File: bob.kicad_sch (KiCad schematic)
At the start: 49 parts, among them J1 Mini USB Female, J2 GPIO (Optional), J3 GPIO (Optional), J4 Screw Terminal, 2.54mm, J5 Conn_01x04_Male, J6 Conn_01x03_Male, U1 W25Q64JVSS, U2 AMS1117-3.3, U3 RP2040, U4 QMI8658C, U5 HP203B, U6 QMC5883L, Y1 12MHz

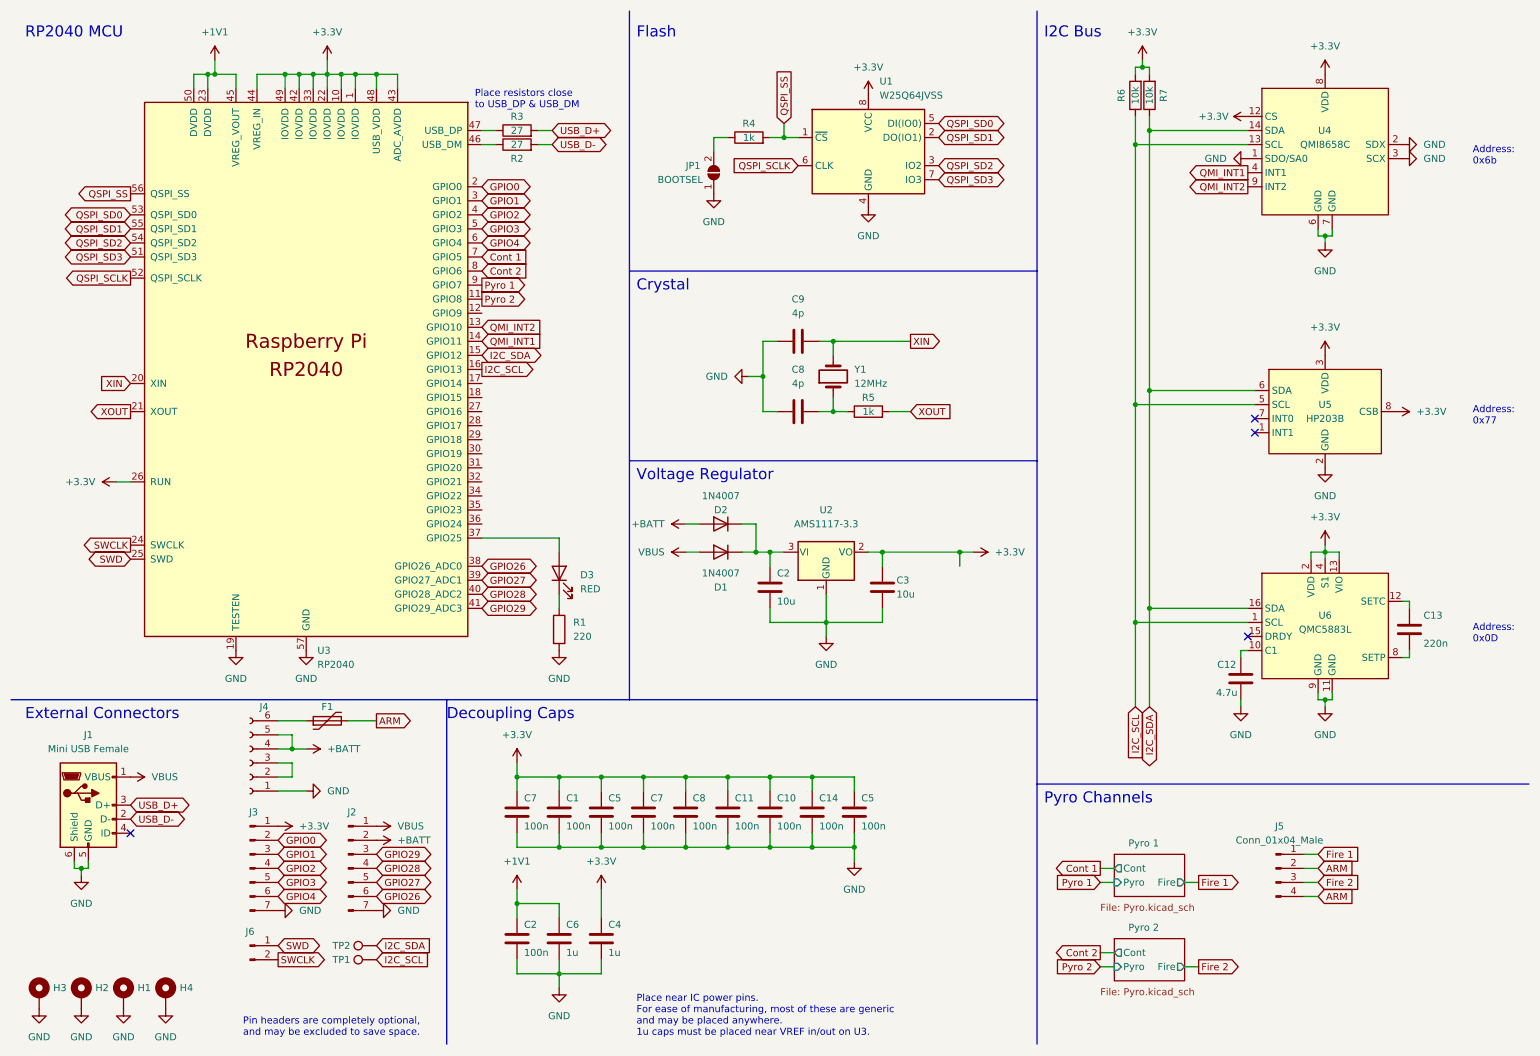
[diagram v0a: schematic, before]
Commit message: Swap out components to match LCSC stock
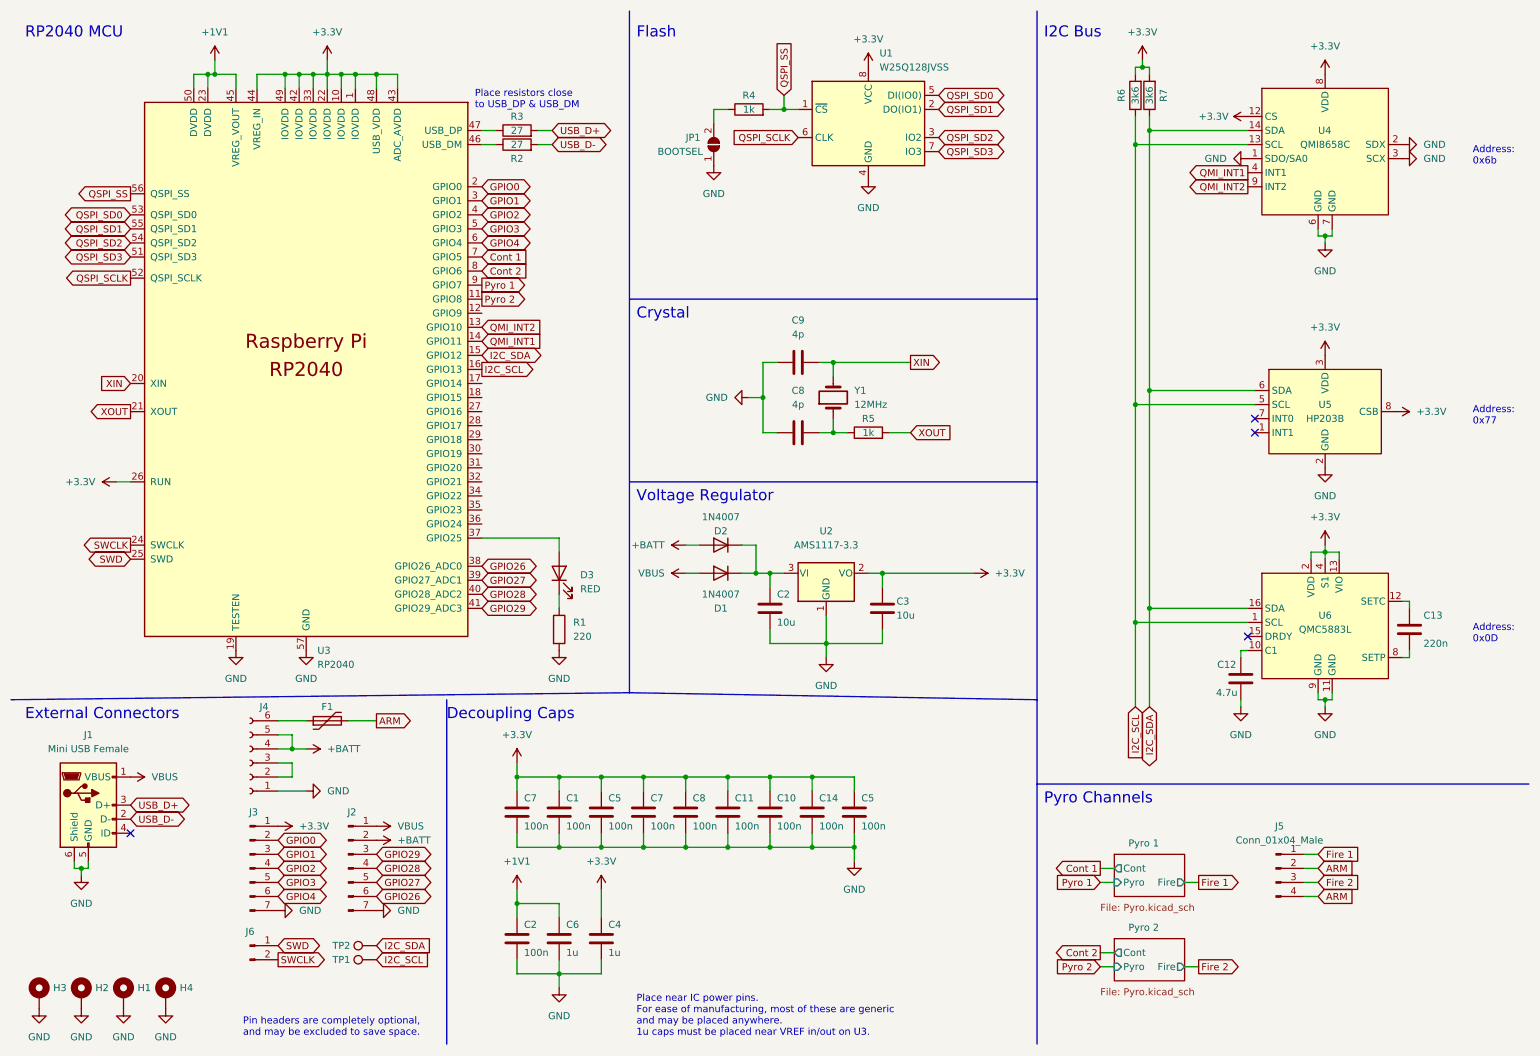
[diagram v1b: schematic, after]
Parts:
- R6, R7: value 10k -> 3k6; LCSC C25804 -> C22980
- U1: value W25Q64JVSS -> W25Q128JVSS; LCSC C83140 -> C97521
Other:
- moved on the sheet: C2, C3, C8, C9, D1, D2, JP1, R4, R5, U1, U2, Y1

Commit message: Add dedicated flash for data
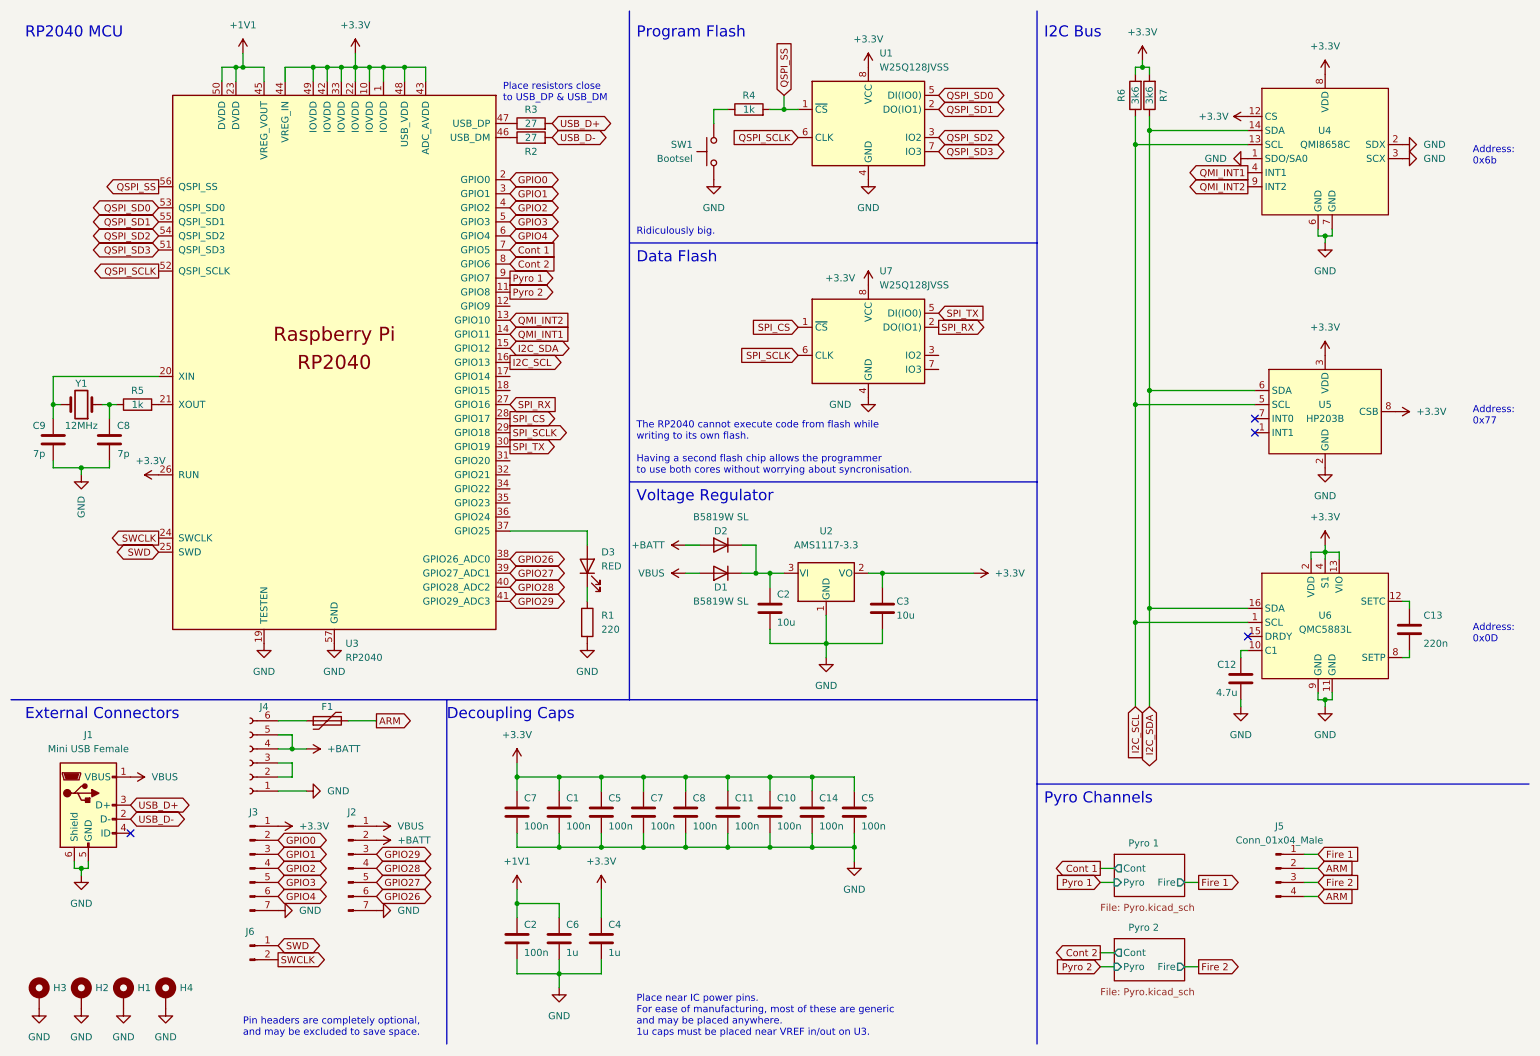
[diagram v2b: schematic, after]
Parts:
- removed JP1: BOOTSEL, Button_Switch_SMD:SW_SPST_B3U-1000P, symbol Jumper:SolderJumper_2_Open
- removed TP1, TP2: TestPoint, TestPoint:TestPoint_Pad_D1.0mm, symbol Connector:TestPoint
- added SW1: Bootsel, Button_Switch_SMD:SW_SPST_TL3342, symbol Switch:SW_Push
- added U7: W25Q128JVSS, Package_SO:SOIC-8_5.23x5.23mm_P1.27mm, symbol Memory_Flash:W25Q32JVSS
- C8, C9: value 4p -> 7p; footprint Capacitor_SMD:C_0603_1608Metric -> Capacitor_SMD:C_0402_1005Metric; JLC 0603 -> 0402; LCSC C2312234 -> C2918529
- D1, D2: value 1N4007 -> B5819W SL; LCSC C727081 -> C8598
- Y1: footprint Crystal:Crystal_SMD_5032-2Pin_5.0x3.2mm -> Crystal:Crystal_SMD_3225-4Pin_3.2x2.5mm; JLC 5032 -> SMD3225-4P
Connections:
- net +3V3: now also U7.8 (VCC)
- net GND: now also SW1.1, U7.4 (GND)
- net at R4.1: now also SW1.2
- net SPI_RX: now reaches U3.27 (GPIO16)
- net SPI_RX: now also U7.2 (DO(IO1))
- net SPI_CS: now reaches U3.28 (GPIO17)
- net SPI_CS: now also U7.1 (~{CS})
- net SPI_SCLK: now reaches U3.29 (GPIO18)
- net SPI_SCLK: now also U7.6 (CLK)
- net SPI_TX: now reaches U3.30 (GPIO19)
- net SPI_TX: now also U7.5 (DI(IO0))
- net XIN: no longer names the net of C9.2, U3.20 (XIN), Y1.2
- net XOUT: no longer names the net of R5.2, U3.21 (XOUT)
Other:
- note added: "Data Flash"
- note added: "Program Flash"
- note added: "Ridiculously big."
- note added: "The RP2040 cannot execute code from flash while writing to its own flash. Having a second flash chip allows the programmer to use both cores without worrying about syncronisation."
- note removed: "Crystal"
- note removed: "Flash"
- moved on the sheet: C8, C9, D3, R1, R2, R3, R5, U3, Y1

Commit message: Return of the buzzer
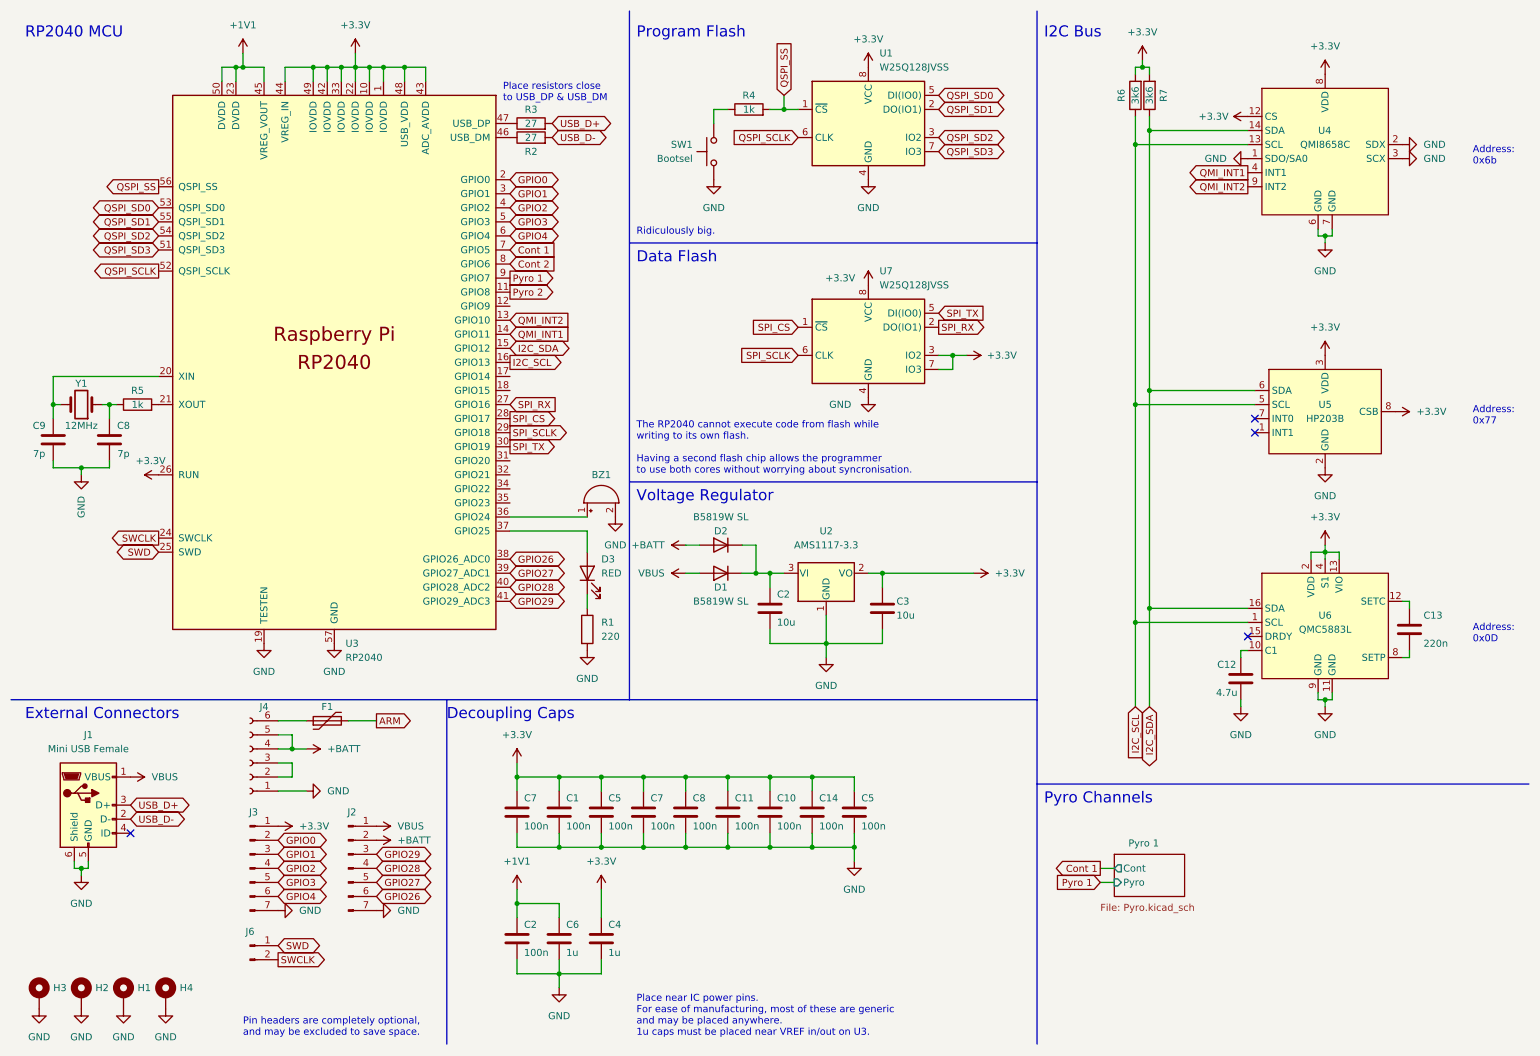
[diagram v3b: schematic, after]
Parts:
- removed J5: Conn_01x04_Male, YAR_Connectors:ScrewTerm_2.54x04, symbol Connector:Conn_01x04_Male
- added BZ1: Buzzer, Buzzer_Beeper:Buzzer_12x9.5RM7.6, symbol Device:Buzzer
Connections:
- net +3V3: now also U7.3 (IO2), U7.7 (IO3)
- net GND: now also BZ1.2 (+)
- net at U3.36 (GPIO24): now also BZ1.1 (-)
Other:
- removed sheet Pyro 2
- sheet Pyro 1 ports: added none; removed Fire
- moved on the sheet: D3, R1

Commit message: Rev 4 issued for production
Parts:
- removed J4: Screw Terminal, 2.54mm, YAR_Connectors:ScrewTerm_2.54x06, symbol Connector:Conn_01x06_Female
- added D4: RED, LED_SMD:LED_0603_1608Metric, symbol Device:LED
- added D5: B5819W SL, Diode_SMD:D_SOD-123, symbol Diode:1N914
- added J2: Screw Terminal, 2.54mm, YAR_Connectors:ScrewTerm_2.54x02, symbol Connector:Conn_01x02_Female
- added J6: Conn_01x06_Pin, YAR_Connectors:ScrewTerm_2.54x06, symbol Connector:Conn_01x06_Pin
- added Q1: AO3400A, Package_TO_SOT_SMD:SOT-23, symbol Transistor_FET:AO3400A
- added R12, R4: 3k6, Resistor_SMD:R_0603_1608Metric, symbol Device:R
- added R9: 470, Resistor_SMD:R_0603_1608Metric, symbol Device:R
- BZ1: footprint Buzzer_Beeper:Buzzer_12x9.5RM7.6 -> YAR_other:Cy-SMD-4020-3040
- D3: value RED -> GREEN
- F1: JLC (none) -> 0603; LCSC (none) -> C2654002
- J1: value Mini USB Female -> Micro USB Female; footprint Connector_USB:USB_Mini-B_Lumberg_2486_01_Horizontal -> Connector_USB:USB_Micro-B_Molex-105017-0001; LCSC C2681563 -> C136000
- J3: renamed from J2; footprint Connector_PinHeader_2.54mm:PinHeader_1x07_P2.54mm_Vertical_NoSilk -> Connector_PinHeader_2.54mm:PinHeader_1x11_P2.54mm_Vertical; symbol Connector:Conn_01x07_Male -> Connector:Conn_01x11_Male
- J4: renamed from J3; footprint Connector_PinHeader_2.54mm:PinHeader_1x07_P2.54mm_Vertical_NoSilk -> Connector_PinHeader_2.54mm:PinHeader_1x11_P2.54mm_Vertical; symbol Connector:Conn_01x07_Male -> Connector:Conn_01x11_Male
- J5: renamed from J6; footprint Connector_PinHeader_2.54mm:PinHeader_1x02_P2.54mm_Vertical -> Connector_PinHeader_2.54mm:PinHeader_1x03_P2.54mm_Vertical; symbol Connector:Conn_01x02_Male -> Connector:Conn_01x03_Male
- U5: renamed from U3; footprint YAR_MCU:RP2040-QFN-56_HS -> YAR_MCU:RP2040-QFN-56
- Y1: symbol Device:Crystal -> Device:Crystal_GND24_Small; LCSC C90884 -> C2838412
- renumbered C9 to C1, C14 to C10, C10 to C11, C1 to C12, C11 to C13, C12 to C14, C13 to C15, C8 to C16, C2 to C17, C3 to C18, C8 to C2, C5 to C3, C7 to C4, C7 to C5, C2 to C6, C4 to C7, C6 to C8, C5 to C9, R2 to R1, R1 to R10, R4 to R11, R3 to R2, R5 to R3, R6 to R7, R7 to R8, U2 to U1, U1 to U2, U6 to U3, U5 to U4, U4 to U6
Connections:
- net +3V3: now also D4.2 (A), D5.1 (K)
- net +BATT: now also BZ1.1 (-), J2.2 (Pin_2), J6.6 (Pin_6)
- net ARM: now also R12.2
- net Cont 1: now also U5.18 (GPIO15); no longer U5.7 (GPIO5)
- net Cont 2: now also U5.17 (GPIO14); no longer U5.8 (GPIO6)
- net GND: now also J3.11 (Pin_11), J4.11 (Pin_11), J5.1 (Pin_1), Y1.2, Y1.4, J2.1 (Pin_1), Q1.2 (S), R9.1; no longer BZ1.2 (+), J3.7 (Pin_7), J4.7 (Pin_7)
- net I2C_SCL: now also J4.10 (Pin_10)
- net I2C_SDA: now also J4.9 (Pin_9)
- net SWCLK: now also J5.3 (Pin_3); no longer J5.2 (Pin_2)
- net SWD: now also J5.2 (Pin_2); no longer J5.1 (Pin_1)
- net at F1.1: now also J6.5 (Pin_5)
- net GPIO24: now reaches U5.36 (GPIO24)
- net GPIO24: now also J3.7 (Pin_7); no longer BZ1.1 (-)
- net at C1.2, U5.20 (XIN): now also Y1.3; no longer Y1.2
- net QMC_DRDY: now reaches U3.15 (DRDY)
- net QMC_DRDY: now also U5.12 (GPIO9)
- net BUZZER: now reaches U5.31 (GPIO20)
- net BUZZER: now also Q1.1 (G)
- net ARMED: now reaches U5.32 (GPIO21)
- net ARMED: now also J3.10 (Pin_10), R4.1
- net GPIO22: now reaches U5.34 (GPIO22)
- net GPIO22: now also J3.9 (Pin_9)
- net GPIO23: now reaches U5.35 (GPIO23)
- net GPIO23: now also J3.8 (Pin_8)
- new net: D5.2 (A), R12.1, R4.2
- new net: BZ1.2 (+), Q1.3 (D)
- new net: D4.1 (K), R9.2
- new net GPIO5: J4.7 (Pin_7), U5.7 (GPIO5)
- new net GPIO6: J4.8 (Pin_8), U5.8 (GPIO6)
- new net Pyro 1/Fire +: J6.4 (Pin_4)
- new net Pyro 1/Fire -: J6.3 (Pin_3)
- new net Pyro 2/Fire +: J6.2 (Pin_2)
- new net Pyro 2/Fire -: J6.1 (Pin_1)
- no-connect marks 4 -> 3
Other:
- added sheet Pyro 2 (Pyro.kicad_sch)
- sheet Pyro 1 ports: added Fire +, Fire -; removed none
- note added: "Buzzer"
- note added: "Ridiculously big. If you can use all this I'll be impressed."
- note removed: "Ridiculously big."
- moved on the sheet: BZ1, C10, C11, C12, C13, C16, C3, C4, C5, C6, C7, C8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
